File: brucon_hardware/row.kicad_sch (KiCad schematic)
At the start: 19 parts

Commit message: Updated bom
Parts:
- D2001, D2002, D2003, D2004, D2005, D2006, D2007, D2008, D2009, D2010, D2011, D2012, D2013, D2014, D2015, D2016, D2017, D2018, D2019: LCSC (none) -> C2874114
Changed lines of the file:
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@@
+      (effects (font (size 1.27 1.27)) hide)
+    )
+    (property "LCSC" "C2874114" (at 61.595 -38.1 0)
       (effects (font (size 1.27 1.27)) hide)
     )
@@
       (effects (font (size 1.27 1.27)) hide)
     )
+    (property "LCSC" "C2874114" (at 61.595 19.05 0)
+      (effects (font (size 1.27 1.27)) hide)
+    )
     (pin "1")
     (pin "2")
@@
       (effects (font (size 1.27 1.27)) hide)
     )
+    (property "LCSC" "C2874114" (at 61.595 -10.16 0)
+      (effects (font (size 1.27 1.27)) hide)
+    )
     (pin "1")
     (pin "2")
@@
       (effects (font (size 1.27 1.27)) hide)
     )
+    (property "LCSC" "C2874114" (at 113.665 19.685 0)
+      (effects (font (size 1.27 1.27)) hide)
+    )
     (pin "1")
     (pin "2")
@@
       (effects (font (size 1.27 1.27)) hide)
     )
+    (property "LCSC" "C2874114" (at 113.665 -37.465 0)
+      (effects (font (size 1.27 1.27)) hide)
+    )
     (pin "4")
     (pin "3")
@@
       (effects (font (size 1.27 1.27)) hide)
     )
+    (property "LCSC" "C2874114" (at 61.595 74.93 0)
+      (effects (font (size 1.27 1.27)) hide)
+    )
     (pin "1")
     (pin "2")
@@
       (effects (font (size 1.27 1.27)) hide)
     )
+    (property "LCSC" "C2874114" (at 87.63 103.505 0)
+      (effects (font (size 1.27 1.27)) hide)
+    )
     (pin "1")
     (pin "2")
@@
       (effects (font (size 1.27 1.27)) hide)
     )
+    (property "LCSC" "C2874114" (at 61.595 132.08 0)
+      (effects (font (size 1.27 1.27)) hide)
+    )
     (pin "1")
     (pin "2")
@@
       (effects (font (size 1.27 1.27)) hide)
     )
+    (property "LCSC" "C2874114" (at 113.665 -9.525 0)
+      (effects (font (size 1.27 1.27)) hide)
+    )
     (pin "1")
     (pin "2")
@@
       (effects (font (size 1.27 1.27)) hide)
     )
+    (property "LCSC" "C2874114" (at 87.63 -37.465 0)
+      (effects (font (size 1.27 1.27)) hide)
+    )
     (pin "4")
     (pin "3")
@@
       (effects (font (size 1.27 1.27)) hide)
     )
+    (property "LCSC" "C2874114" (at 87.63 19.685 0)
+      (effects (font (size 1.27 1.27)) hide)
+    )
     (pin "1")
     (pin "2")
@@
       (effects (font (size 1.27 1.27)) hide)
     )
+    (property "LCSC" "C2874114" (at 87.63 160.655 0)
+      (effects (font (size 1.27 1.27)) hide)
+    )
     (pin "1")
     (pin "2")
@@
       (effects (font (size 1.27 1.27)) hide)
     )
+    (property "LCSC" "C2874114" (at 87.63 75.565 0)
+      (effects (font (size 1.27 1.27)) hide)
+    )
     (pin "1")
     (pin "2")
@@
       (effects (font (size 1.27 1.27)) hide)
     )
+    (property "LCSC" "C2874114" (at 61.595 102.87 0)
+      (effects (font (size 1.27 1.27)) hide)
+    )
     (pin "1")
     (pin "2")
@@
       (effects (font (size 1.27 1.27)) hide)
     )
+    (property "LCSC" "C2874114" (at 87.63 47.625 0)
+      (effects (font (size 1.27 1.27)) hide)
+    )
     (pin "1")
     (pin "2")
@@
       (effects (font (size 1.27 1.27)) hide)
     )
+    (property "LCSC" "C2874114" (at 61.595 46.99 0)
+      (effects (font (size 1.27 1.27)) hide)
+    )
     (pin "1")
     (pin "2")
@@
       (effects (font (size 1.27 1.27)) hide)
     )
+    (property "LCSC" "C2874114" (at 61.595 160.02 0)
+      (effects (font (size 1.27 1.27)) hide)
+    )
     (pin "1")
     (pin "2")
@@
       (effects (font (size 1.27 1.27)) hide)
     )
+    (property "LCSC" "C2874114" (at 87.63 132.715 0)
+      (effects (font (size 1.27 1.27)) hide)
+    )
     (pin "1")
     (pin "2")
@@
       (effects (font (size 1.27 1.27)) hide)
     )
+    (property "LCSC" "C2874114" (at 87.63 -9.525 0)
+      (effects (font (size 1.27 1.27)) hide)
+    )

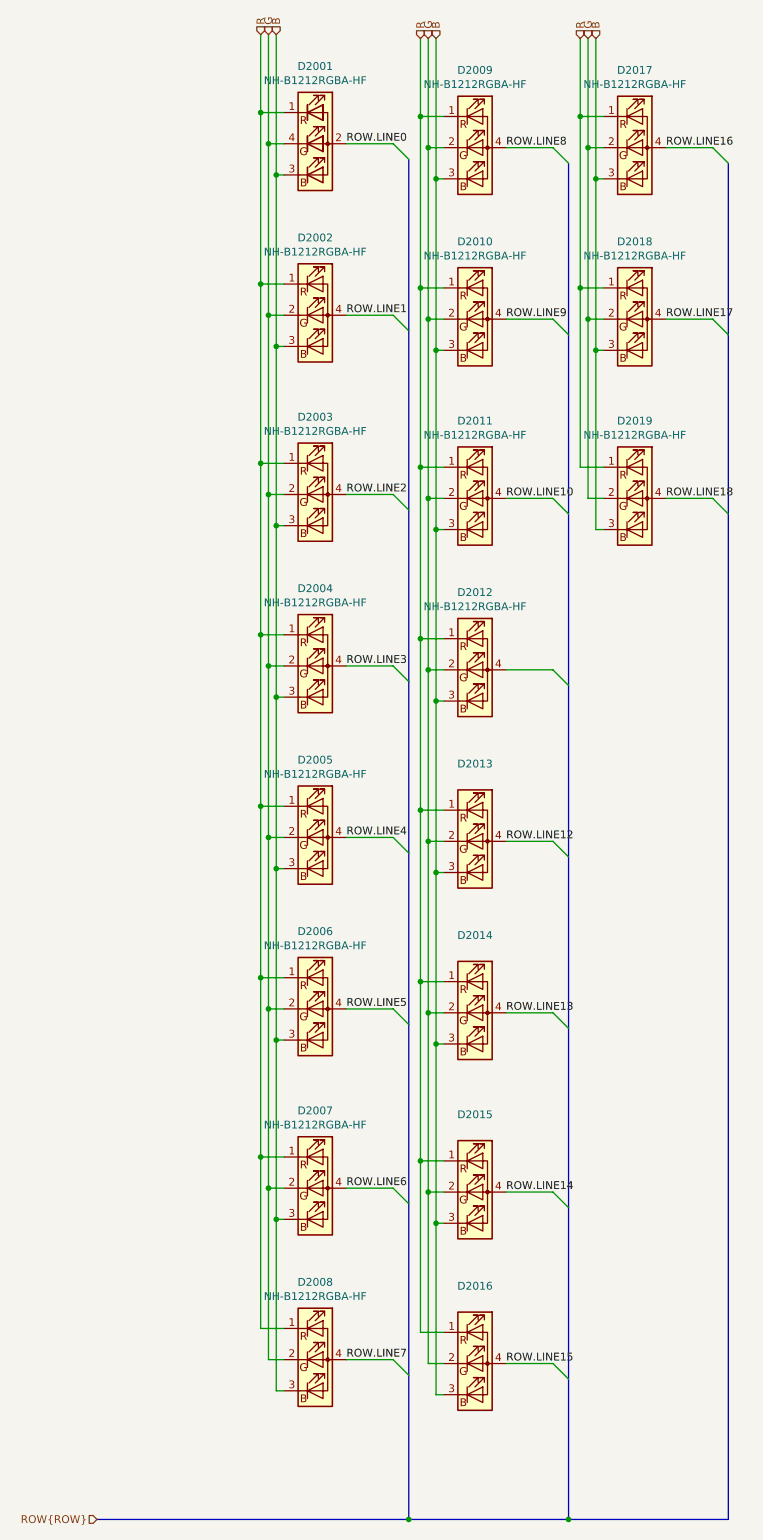
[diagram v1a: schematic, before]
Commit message: Initial led matrix placement
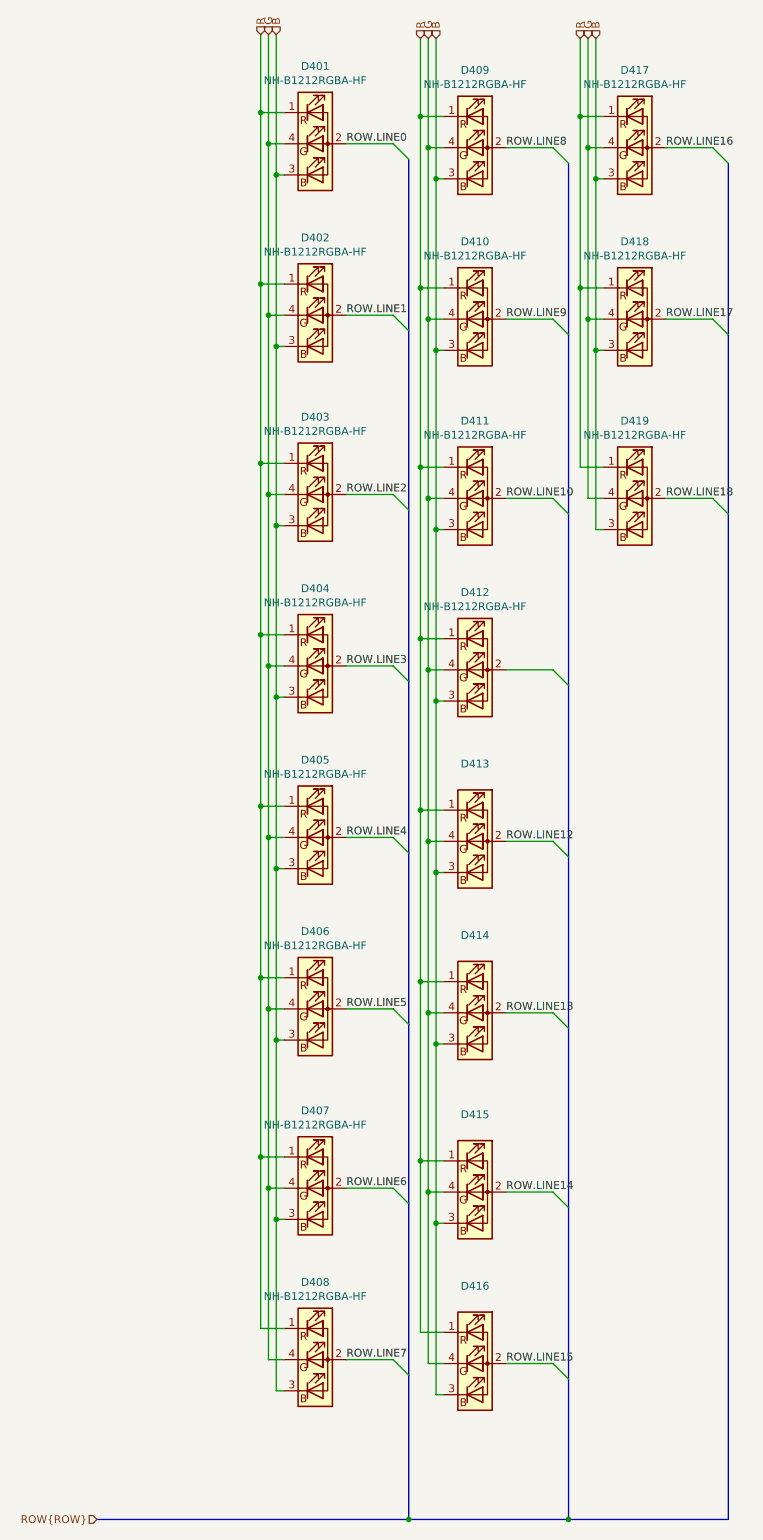
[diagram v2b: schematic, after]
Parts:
- D402: renamed from D2002; symbol led_rgba:LED_RGBA -> Device:LED_RABG
- D403: renamed from D2003; symbol led_rgba:LED_RGBA -> Device:LED_RABG
- D404: renamed from D2004; symbol led_rgba:LED_RGBA -> Device:LED_RABG
- D405: renamed from D2005; symbol led_rgba:LED_RGBA -> Device:LED_RABG
- D406: renamed from D2006; symbol led_rgba:LED_RGBA -> Device:LED_RABG
- D407: renamed from D2007; symbol led_rgba:LED_RGBA -> Device:LED_RABG
- D408: renamed from D2008; symbol led_rgba:LED_RGBA -> Device:LED_RABG
- D409: renamed from D2009; symbol led_rgba:LED_RGBA -> Device:LED_RABG
- D410: renamed from D2010; symbol led_rgba:LED_RGBA -> Device:LED_RABG
- D411: renamed from D2011; symbol led_rgba:LED_RGBA -> Device:LED_RABG
- D412: renamed from D2012; symbol led_rgba:LED_RGBA -> Device:LED_RABG
- D413: renamed from D2013; symbol led_rgba:LED_RGBA -> Device:LED_RABG
- D414: renamed from D2014; symbol led_rgba:LED_RGBA -> Device:LED_RABG
- D415: renamed from D2015; symbol led_rgba:LED_RGBA -> Device:LED_RABG
- D416: renamed from D2016; symbol led_rgba:LED_RGBA -> Device:LED_RABG
- D417: renamed from D2017; symbol led_rgba:LED_RGBA -> Device:LED_RABG
- D418: renamed from D2018; symbol led_rgba:LED_RGBA -> Device:LED_RABG
- D419: renamed from D2019; symbol led_rgba:LED_RGBA -> Device:LED_RABG
- renumbered D2001 to D401
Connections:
- net G: now also D402.4 (GK), D403.4 (GK), D404.4 (GK), D405.4 (GK), D406.4 (GK), D407.4 (GK), D408.4 (GK), D409.4 (GK), D410.4 (GK), D411.4 (GK), D412.4 (GK), D413.4 (GK), D414.4 (GK), D415.4 (GK), D416.4 (GK), D417.4 (GK), D418.4 (GK), D419.4 (GK); no longer D402.2 (RK), D403.2 (RK), D404.2 (RK), D405.2 (RK), D406.2 (RK), D407.2 (RK), D408.2 (RK), D409.2 (RK), D410.2 (RK), D411.2 (RK), D412.2 (RK), D413.2 (RK), D414.2 (RK), D415.2 (RK), D416.2 (RK), D417.2 (RK), D418.2 (RK), D419.2 (RK)
- net ROW.LINE1: now also D402.2 (A); no longer D402.4 (BK)
- net ROW.LINE10: now also D411.2 (A); no longer D411.4 (BK)
- net ROW.LINE12: now also D413.2 (A); no longer D413.4 (BK)
- net ROW.LINE13: now also D414.2 (A); no longer D414.4 (BK)
- net ROW.LINE14: now also D415.2 (A); no longer D415.4 (BK)
- net ROW.LINE15: now also D416.2 (A); no longer D416.4 (BK)
- net ROW.LINE16: now also D417.2 (A); no longer D417.4 (BK)
- net ROW.LINE17: now also D418.2 (A); no longer D418.4 (BK)
- net ROW.LINE18: now also D419.2 (A); no longer D419.4 (BK)
- net ROW.LINE2: now also D403.2 (A); no longer D403.4 (BK)
- net ROW.LINE3: now also D404.2 (A); no longer D404.4 (BK)
- net ROW.LINE4: now also D405.2 (A); no longer D405.4 (BK)
- net ROW.LINE5: now also D406.2 (A); no longer D406.4 (BK)
- net ROW.LINE6: now also D407.2 (A); no longer D407.4 (BK)
- net ROW.LINE7: now also D408.2 (A); no longer D408.4 (BK)
- net ROW.LINE8: now also D409.2 (A); no longer D409.4 (BK)
- net ROW.LINE9: now also D410.2 (A); no longer D410.4 (BK)

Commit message: Finished major parts routing led matrix
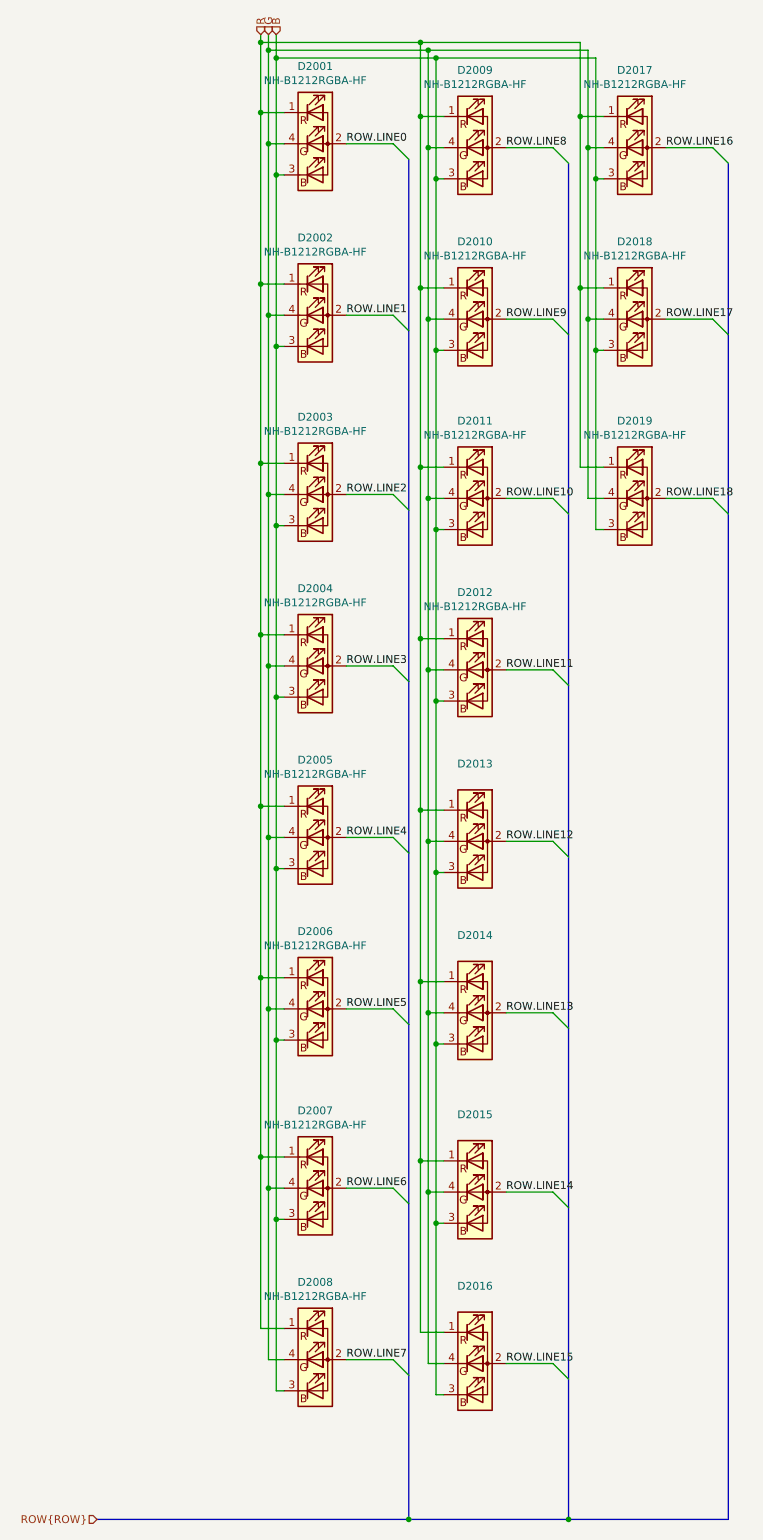
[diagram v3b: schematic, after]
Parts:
- renumbered D401 to D2001, D402 to D2002, D403 to D2003, D404 to D2004, D405 to D2005, D406 to D2006, D407 to D2007, D408 to D2008, D409 to D2009, D410 to D2010, D411 to D2011, D412 to D2012, D413 to D2013, D414 to D2014, D415 to D2015, D416 to D2016, D417 to D2017, D418 to D2018, D419 to D2019
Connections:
- net ROW.LINE11: now reaches D2012.2 (A)

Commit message: Updated to kicad v8
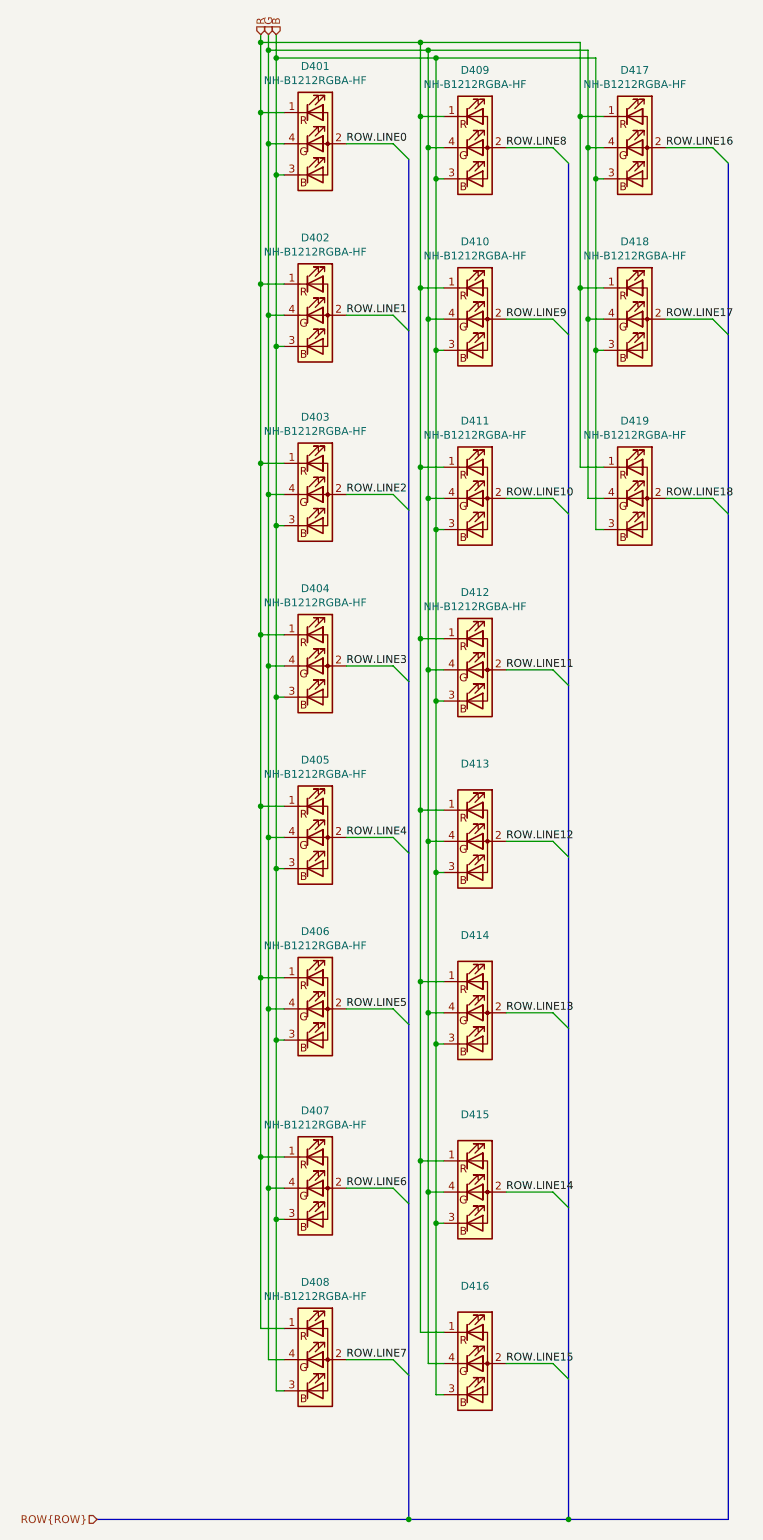
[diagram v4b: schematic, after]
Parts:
- renumbered D2001 to D401, D2002 to D402, D2003 to D403, D2004 to D404, D2005 to D405, D2006 to D406, D2007 to D407, D2008 to D408, D2009 to D409, D2010 to D410, D2011 to D411, D2012 to D412, D2013 to D413, D2014 to D414, D2015 to D415, D2016 to D416, D2017 to D417, D2018 to D418, D2019 to D419

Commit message: Fixed DRC errors
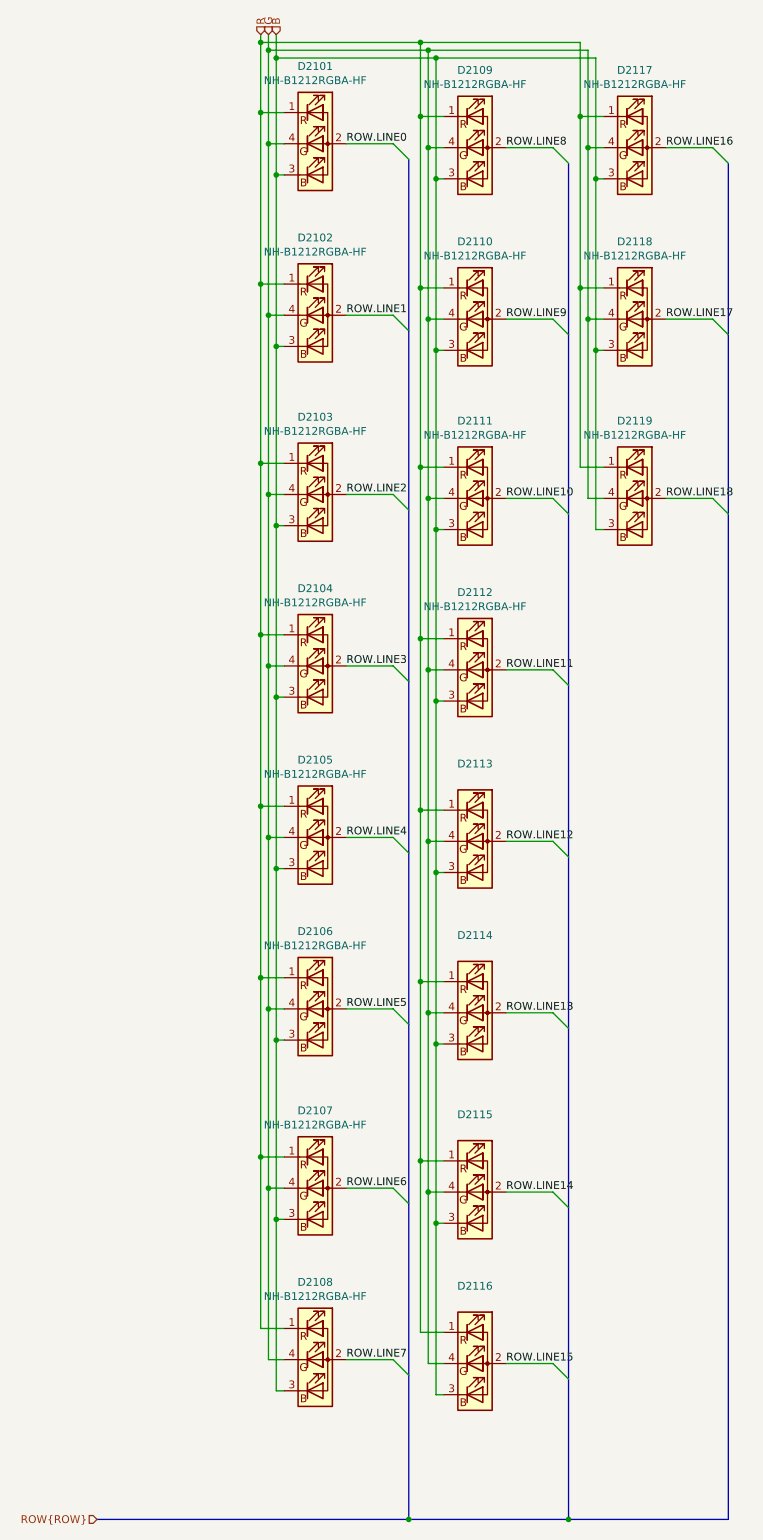
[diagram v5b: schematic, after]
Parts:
- renumbered D401 to D2101, D402 to D2102, D403 to D2103, D404 to D2104, D405 to D2105, D406 to D2106, D407 to D2107, D408 to D2108, D409 to D2109, D410 to D2110, D411 to D2111, D412 to D2112, D413 to D2113, D414 to D2114, D415 to D2115, D416 to D2116, D417 to D2117, D418 to D2118, D419 to D2119
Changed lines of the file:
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@@
 		(on_board yes)
 		(dnp no)
-		(property "Reference" "D401"
+		(property "Reference" "D2101"
 			(at 61.595 -50.7238 0)
 			(effects
@@
 		(on_board yes)
 		(dnp no)
-		(property "Reference" "D403"
+		(property "Reference" "D2103"
 			(at 61.595 6.4262 0)
 			(effects
@@
 		(on_board yes)
 		(dnp no)
-		(property "Reference" "D402"
+		(property "Reference" "D2102"
 			(at 61.595 -22.7838 0)
 			(effects
@@
 		(on_board yes)
 		(dnp no)
-		(property "Reference" "D419"
+		(property "Reference" "D2119"
 			(at 113.665 7.0612 0)
 			(effects
@@
 		(on_board yes)
 		(dnp no)
-		(property "Reference" "D417"
+		(property "Reference" "D2117"
 			(at 113.665 -50.0888 0)
 			(effects
@@
 		(on_board yes)
 		(dnp no)
-		(property "Reference" "D405"
+		(property "Reference" "D2105"
 			(at 61.595 62.3062 0)
 			(effects
@@
 		(on_board yes)
 		(dnp no)
-		(property "Reference" "D414"
+		(property "Reference" "D2114"
 			(at 87.63 90.8812 0)
 			(effects
@@
 		(on_board yes)
 		(dnp no)
-		(property "Reference" "D407"
+		(property "Reference" "D2107"
 			(at 61.595 119.4562 0)
 			(effects
@@
 		(on_board yes)
 		(dnp no)
-		(property "Reference" "D418"
+		(property "Reference" "D2118"
 			(at 113.665 -22.1488 0)
 			(effects
@@
 		(on_board yes)
 		(dnp no)
-		(property "Reference" "D409"
+		(property "Reference" "D2109"
 			(at 87.63 -50.0888 0)
 			(effects
@@
 		(on_board yes)
 		(dnp no)
-		(property "Reference" "D411"
+		(property "Reference" "D2111"
 			(at 87.63 7.0612 0)
 			(effects
@@
 		(on_board yes)
 		(dnp no)
-		(property "Reference" "D416"
+		(property "Reference" "D2116"
 			(at 87.63 148.0312 0)
 			(effects
@@
 		(on_board yes)
 		(dnp no)
-		(property "Reference" "D413"
+		(property "Reference" "D2113"
 			(at 87.63 62.9412 0)
 			(effects
@@
 		(on_board yes)
 		(dnp no)
-		(property "Reference" "D406"
+		(property "Reference" "D2106"
 			(at 61.595 90.2462 0)
 			(effects
@@
 		(on_board yes)
 		(dnp no)
-		(property "Reference" "D412"
+		(property "Reference" "D2112"
 			(at 87.63 35.0012 0)
 			(effects
@@
 		(on_board yes)
 		(dnp no)
-		(property "Reference" "D404"
+		(property "Reference" "D2104"
 			(at 61.595 34.3662 0)
 			(effects
@@
 		(on_board yes)
 		(dnp no)
-		(property "Reference" "D408"
+		(property "Reference" "D2108"
 			(at 61.595 147.3962 0)
 			(effects
@@
 		(on_board yes)
 		(dnp no)
-		(property "Reference" "D415"
+		(property "Reference" "D2115"
 			(at 87.63 120.0912 0)
 			(effects
@@
 		(on_board yes)
 		(dnp no)
-		(property "Reference" "D410"
+		(property "Reference" "D2110"
 			(at 87.63 -22.1488 0)
 			(effects
